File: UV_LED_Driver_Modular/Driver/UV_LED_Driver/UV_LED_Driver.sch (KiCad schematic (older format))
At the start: 1 part, among them J1 Conn_02x06_Odd_Even

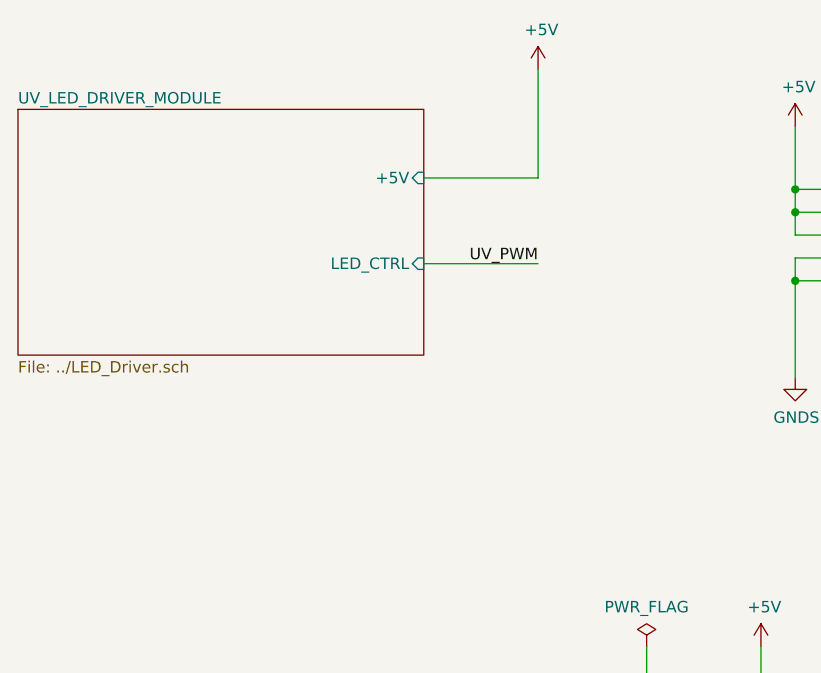
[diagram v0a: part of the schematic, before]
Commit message: Changed TO225 NPN (MJE340) to SOT223 NPN (PZT2222A)
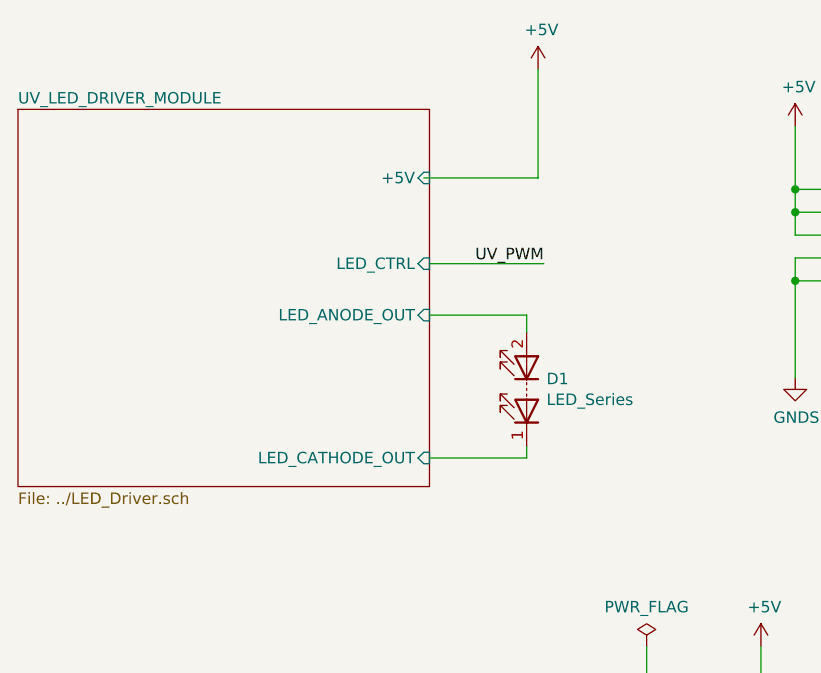
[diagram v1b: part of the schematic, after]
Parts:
- added D1: LED_Series, Connector_Molex_MiniFitJnrExtra:Molex_Mini-Fit_Jr_5569-06A2_2x03_P4.20mm_Horizontal, symbol Device:LED_Series
- J1: footprint (none) -> Connector_IDC:IDC-Header_2x06_P2.54mm_Vertical
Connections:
- wire segments 27 -> 31
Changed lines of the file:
@@
 $EndDescr
 $Sheet
-S 2700 2925 1775 1075
+S 2700 2925 1800 1650
 U 5EA57624
 F0 "UV_LED_DRIVER_MODULE" 50
 F1 "../LED_Driver.sch" 50
-F2 "+5V" I R 4475 3225 50
-F3 "LED_CTRL" I R 4475 3600 50
+F2 "+5V" I R 4500 3225 50
+F3 "LED_CTRL" I R 4500 3600 50
+F4 "LED_ANODE_OUT" I R 4500 3825 50
+F5 "LED_CATHODE_OUT" I R 4500 4450 50
 $EndSheet
 Wire Wire Line
 	4475 3225 4975 3225
 Wire Wire Line
-	4475 3600 4975 3600
+	4500 3600 5000 3600
 Wire Wire Line
 	4975 3225 4975 2750
@@
 	1    0    0    -1
 $EndComp
-Text Label 4975 3600 2    50   ~ 0
+Text Label 5000 3600 2    50   ~ 0
 UV_PWM
 $Comp
@@
 F 0 "J1" H 7025 3892 50  0000 C CNN
 F 1 "Conn_02x06_Odd_Even" H 7025 3801 50  0000 C CNN
-F 2 "" H 6975 3475 50  0001 C CNN
+F 2 "Connector_IDC:IDC-Header_2x06_P2.54mm_Vertical" H 6975 3475 50  0001 C CNN
 F 3 "~" H 6975 3475 50  0001 C CNN
 	1    6975 3475
@@
 UV_PWM
 $Comp
-L power:PWR_FLAG #FLG?
+L power:PWR_FLAG #FLG0101
 U 1 1 5EA6A5EB
 P 5450 5275
-F 0 "#FLG?" H 5450 5350 50  0001 C CNN
+F 0 "#FLG0101" H 5450 5350 50  0001 C CNN
 F 1 "PWR_FLAG" H 5450 5448 50  0000 C CNN
 F 2 "" H 5450 5275 50  0001 C CNN
@@
 $EndComp
 $Comp
-L power:PWR_FLAG #FLG?
+L power:PWR_FLAG #FLG0102
 U 1 1 5EA6A68B
 P 5950 5775
-F 0 "#FLG?" H 5950 5850 50  0001 C CNN
+F 0 "#FLG0102" H 5950 5850 50  0001 C CNN
 F 1 "PWR_FLAG" H 5950 5948 50  0000 C CNN
 F 2 "" H 5950 5775 50  0001 C CNN
@@
 $EndComp
 $Comp
-L power:+5V #PWR?
+L power:+5V #PWR0103
 U 1 1 5EA6A991
 P 5950 5275
-F 0 "#PWR?" H 5950 5125 50  0001 C CNN
+F 0 "#PWR0103" H 5950 5125 50  0001 C CNN
 F 1 "+5V" H 5965 5448 50  0000 C CNN
 F 2 "" H 5950 5275 50  0001 C CNN
@@
 	5950 5275 5950 5775
 $Comp
-L power:GNDS #PWR?
+L power:GNDS #PWR0104
 U 1 1 5EA6AF84
 P 5450 5775
-F 0 "#PWR?" H 5450 5525 50  0001 C CNN
+F 0 "#PWR0104" H 5450 5525 50  0001 C CNN
 F 1 "GNDS" H 5455 5602 50  0000 C CNN
 F 2 "" H 5450 5775 50  0001 C CNN
@@
 Wire Wire Line
 	5450 5275 5450 5775
+$Comp
+L Device:LED_Series D1
+U 1 1 5EA4E981
+P 4925 4150
+F 0 "D1" V 4971 4063 50  0000 R CNN
+F 1 "LED_Series" V 4880 4063 50  0000 R CNN
+F 2 "Connector_Molex_MiniFitJnrExtra:Molex_Mini-Fit_Jr_5569-06A2_2x03_P4.20mm_Horizontal" H 4825 4150 50  0001 C CNN
+F 3 "~" H 4825 4150 50  0001 C CNN
+	1    4925 4150
+	0    -1   -1   0
+$EndComp
+Wire Wire Line
+	4500 3825 4925 3825
+Wire Wire Line
+	4925 3825 4925 3900
+Wire Wire Line
+	4500 4450 4925 4450
+Wire Wire Line
+	4925 4450 4925 4400
 $EndSCHEMATC

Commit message: docs update
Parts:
- removed J1: Conn_02x06_Odd_Even, Connector_IDC:IDC-Header_2x06_P2.54mm_Vertical, symbol Connector_Generic:Conn_02x06_Odd_Even
- added J1: Conn_02x08_Odd_Even, Connector_PinHeader_2.54mm:PinHeader_2x08_P2.54mm_Vertical, symbol Connector_Generic:Conn_02x08_Odd_Even
- added J2: Conn_02x05_Odd_Even, Connector_PinHeader_2.54mm:PinHeader_2x05_P2.54mm_Vertical, symbol Connector_Generic:Conn_02x05_Odd_Even
- D1: footprint Connector_Molex_MiniFitJnrExtra:Molex_Mini-Fit_Jr_5569-06A2_2x03_P4.20mm_Horizontal -> Connector_Molex:Molex_Mini-Fit_Jr_5569-02A2_2x01_P4.20mm_Horizontal
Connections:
- net labels added: LED_PWM_OUT1, LED_PWM_OUT2, LED_PWM_OUT3, LED_PWM_OUT4, LED_PWM_OUT5, VPP
- net labels removed: +5V
- wire segments 31 -> 48
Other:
- moved on the sheet: D1

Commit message: hw update
modified output pin header
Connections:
- net LED_PWM_OUT5: now also J1.6 (Pin_6)
- no-connect marks 1 -> 0
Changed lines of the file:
@@
 LED_PWM_OUT4
 Wire Wire Line
-	3450 3375 4175 3375
+	2950 3375 2225 3375
 Wire Wire Line
 	3450 3475 4325 3475
@@
 	4325 3675 3450 3675
 Connection ~ 4325 3575
-NoConn ~ 2950 3375
 Wire Wire Line
 	2950 3475 1975 3475
@@
 Text Label 4175 3175 2    50   ~ 0
 LED_PWM_OUT3
+Text Label 2225 3375 0    50   ~ 0
+LED_PWM_OUT5
+Wire Wire Line
+	3450 3375 4175 3375
 Text Label 4175 3375 2    50   ~ 0
 LED_PWM_OUT5

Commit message: Updated prototype designs for fab
updated readme
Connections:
- net LED_PWM_OUT1: now also J1.3 (Pin_3), J2.10 (Pin_10); no longer J1.4 (Pin_4), J2.2 (Pin_2)
- net LED_PWM_OUT2: now also J1.1 (Pin_1), J2.8 (Pin_8); no longer J1.2 (Pin_2), J2.4 (Pin_4)
- net LED_PWM_OUT3: now also J1.2 (Pin_2); no longer J1.1 (Pin_1)
- net LED_PWM_OUT4: now also J1.4 (Pin_4), J2.4 (Pin_4); no longer J1.3 (Pin_3), J2.8 (Pin_8)
- net LED_PWM_OUT5: now also J2.2 (Pin_2); no longer J1.5 (Pin_5), J2.10 (Pin_10)
- no-connect marks 0 -> 1
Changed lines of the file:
@@
 Comment4 ""
 $EndDescr
-$Sheet
-S 8000 2750 1800 1650
-U 5EA57624
-F0 "UV_LED_DRIVER_MODULE" 50
-F1 "../LED_Driver.sch" 50
-F2 "LED_CTRL" I L 8000 3425 50
-F3 "LED_ANODE_OUT" I L 8000 3650 50
-F4 "LED_CATHODE_OUT" I L 8000 4275 50
-F5 "VPP" I L 8000 3050 50
-$EndSheet
 Text Label 7500 3425 0    50   ~ 0
 UV_PWM
@@
 $EndComp
 Wire Wire Line
-	3450 3175 4175 3175
-Wire Wire Line
-	3450 3275 4175 3275
+	2950 3175 2225 3175
+Wire Wire Line
+	2950 3275 2225 3275
+Text Label 5425 3525 0    50   ~ 0
+LED_PWM_OUT2
+Wire Wire Line
+	5425 3325 6225 3325
+Wire Wire Line
+	6225 3225 5425 3225
 Text Label 5425 3325 0    50   ~ 0
-LED_PWM_OUT2
-Wire Wire Line
-	5425 3325 6225 3325
-Wire Wire Line
-	6225 3225 5425 3225
-Text Label 5425 3525 0    50   ~ 0
 LED_PWM_OUT4
 Wire Wire Line
@@
 Wire Wire Line
 	6225 3425 5425 3425
-Text Label 5425 3225 0    50   ~ 0
+Text Label 5425 3625 0    50   ~ 0
 LED_PWM_OUT1
 Wire Wire Line
@@
 Wire Wire Line
 	6225 3625 5425 3625
-Text Label 5425 3625 0    50   ~ 0
+Text Label 5425 3225 0    50   ~ 0
 LED_PWM_OUT5
 Wire Wire Line
@@
 $EndComp
 Wire Wire Line
-	2950 3175 2225 3175
-Wire Wire Line
-	2950 3275 2225 3275
+	3450 3175 4175 3175
+Wire Wire Line
+	4175 3275 3450 3275
 $Comp
 L power:VPP #PWR0103
@@
 Wire Wire Line
 	7525 3050 8000 3050
+Text Label 4175 3175 2    50   ~ 0
+LED_PWM_OUT2
+Text Label 2225 3275 0    50   ~ 0
+LED_PWM_OUT4
+Text Label 4175 3275 2    50   ~ 0
+LED_PWM_OUT1
 Text Label 2225 3175 0    50   ~ 0
-LED_PWM_OUT2
-Text Label 4175 3275 2    50   ~ 0
-LED_PWM_OUT4
-Text Label 2225 3275 0    50   ~ 0
-LED_PWM_OUT1
-Text Label 4175 3175 2    50   ~ 0
 LED_PWM_OUT3
+$Sheet
+S 8000 2750 1800 1650
+U 5EA57624
+F0 "UV_LED_DRIVER_MODULE" 50
+F1 "LED_Driver.sch" 50
+F2 "LED_CTRL" I L 8000 3425 50
+F3 "LED_ANODE_OUT" I L 8000 3650 50
+F4 "LED_CATHODE_OUT" I L 8000 4275 50
+F5 "VPP" I L 8000 3050 50
+$EndSheet
 Text Label 2225 3375 0    50   ~ 0
 LED_PWM_OUT5
-Wire Wire Line
-	3450 3375 4175 3375
-Text Label 4175 3375 2    50   ~ 0
-LED_PWM_OUT5
+NoConn ~ 3450 3375
 $EndSCHEMATC
